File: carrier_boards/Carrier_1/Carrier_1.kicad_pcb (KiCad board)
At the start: 2 copper layers, 44 x 44 mm, 11 parts, among them J5 HV, U2 SHT30-DIS

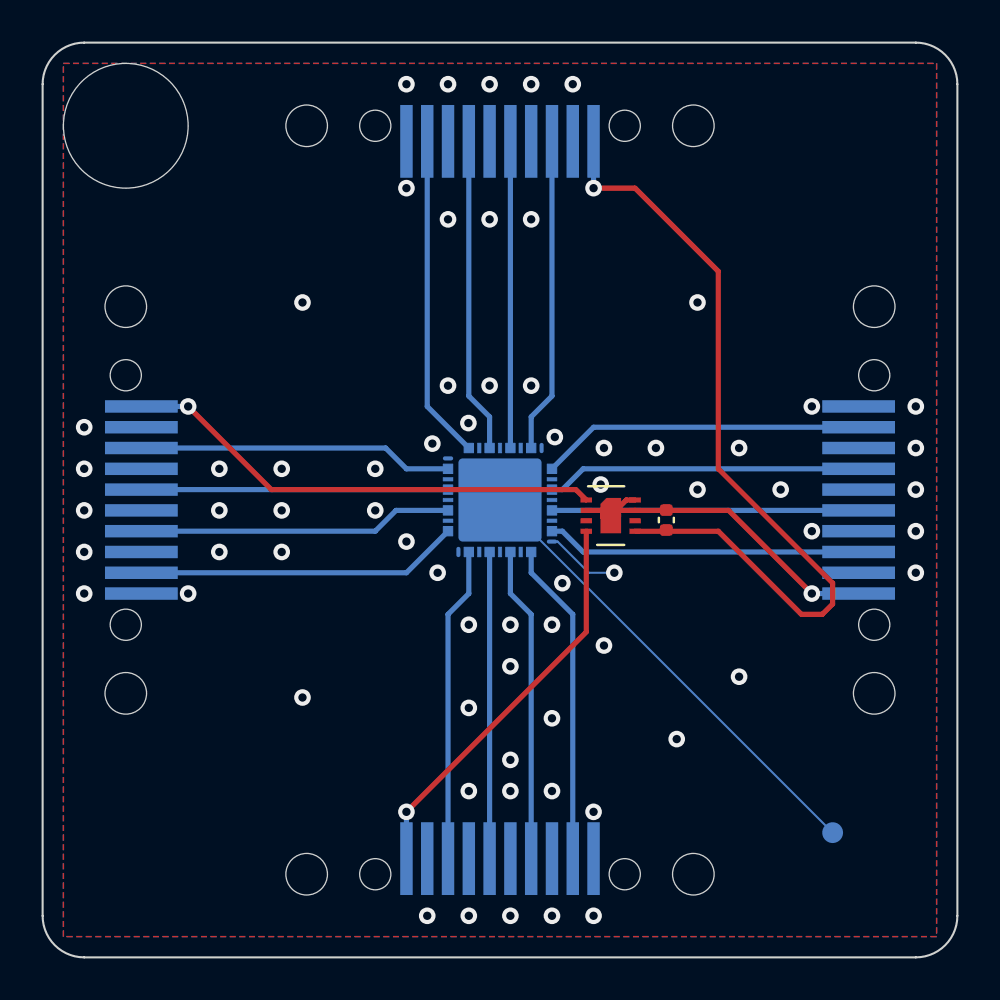
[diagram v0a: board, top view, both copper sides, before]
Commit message: New version, DUT rotated 45 deg and slightly more space for BNL sensors
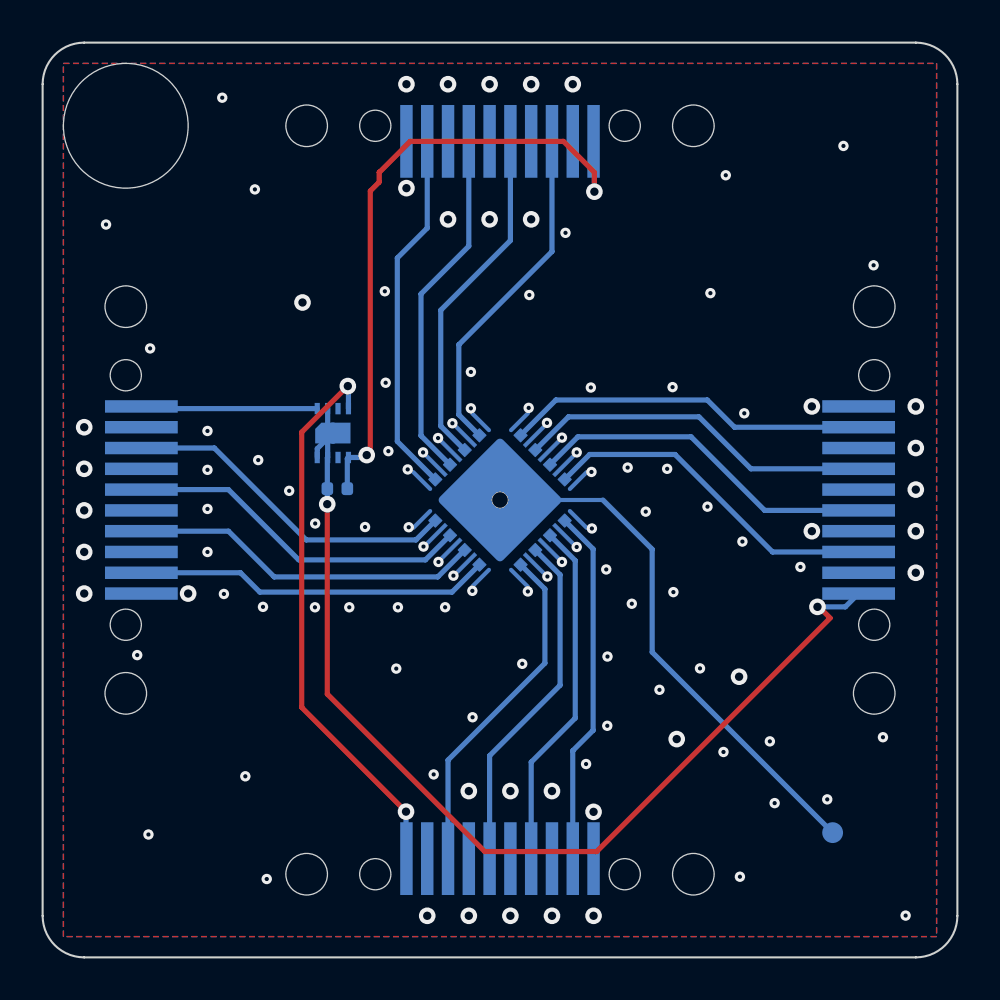
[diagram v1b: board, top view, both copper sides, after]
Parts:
- C1, U2: moved to B.Cu
- moved C1 15.9 mm to (-7.83, -0.55), turned to 180 degrees
- moved U2 13.9 mm to (-8.04, -3.22), turned to -90 degrees
- moved G*** 2.48 mm to (-2.33, 0.65)
- moved G*** 2.19 mm to (-0.08, 2.19)
- turned U1 to 45 degrees
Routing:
- net /I2C_GND: track 16.4 -> 49.8 mm, vias 1 -> 2
- net /SDA: track 23.3 -> 8.50 mm, vias 1 -> 0
- net /I2C_POWER: track 39.5 -> 31.2 mm, vias 1 -> 2
- net /SCL: track 19.3 -> 26.8 mm, vias 1 -> 2
- net GND: track 3.62 -> 0.00 mm, vias 68 -> 114
- net /HV: track 22.6 -> 25.6 mm, vias 0 -> 1
- net Net-(U1-1,3): track 14.8 -> 16.9 mm
- net Net-(U1-2,3): track 15.2 -> 17.2 mm
- net Net-(U1-2,1): track 15.6 -> 17.6 mm
- net Net-(U1-0,1): track 14.8 -> 16.7 mm
- net Net-(U1-2,0): track 14.8 -> 16.7 mm
- net Net-(U1-2,2): track 14.8 -> 16.7 mm
- net Net-(U1-3,3): track 15.6 -> 17.5 mm
- net Net-(U1-3,1): track 15.2 -> 17.1 mm
- net Net-(U1-1,0): track 15.2 -> 17.0 mm
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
